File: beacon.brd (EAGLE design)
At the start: 40 x 23.2 mm, 23 parts, among them IC1 MEGA48/88/168-AU, X1 MINI-USB-SCHIELD-32005-301

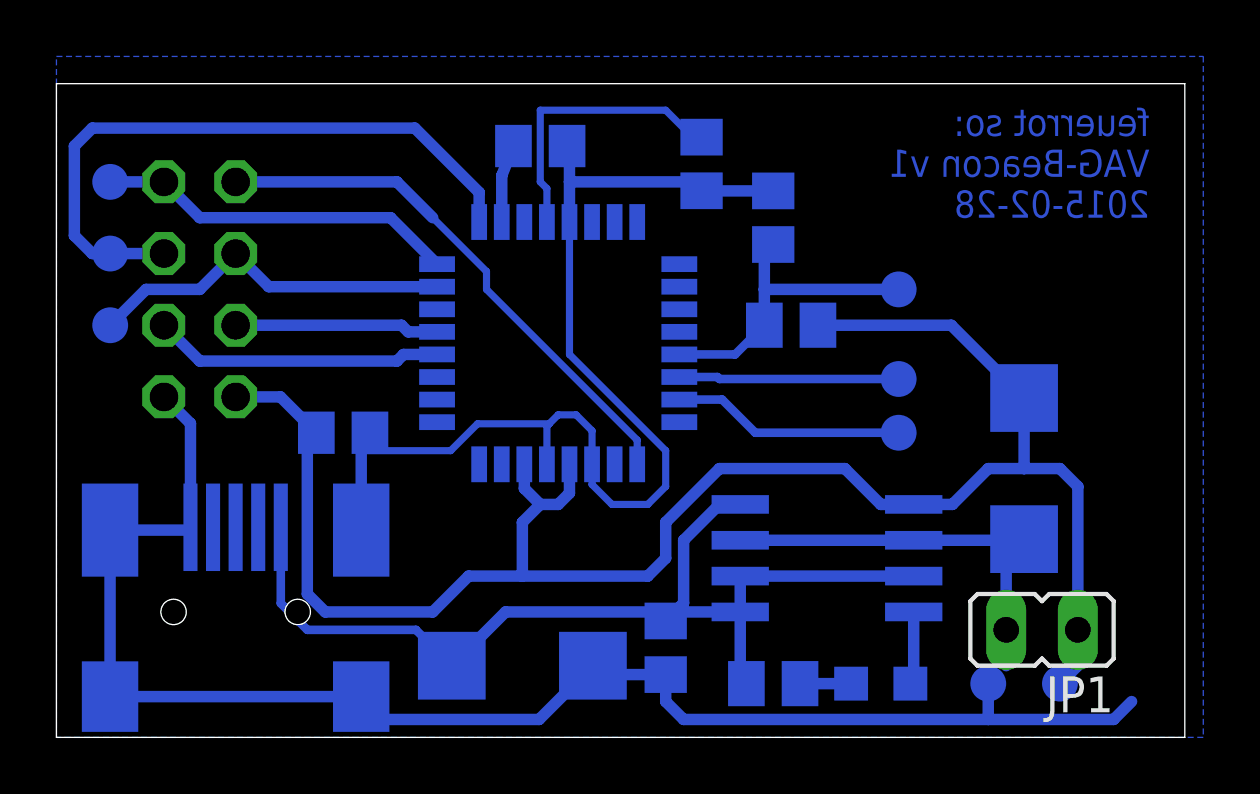
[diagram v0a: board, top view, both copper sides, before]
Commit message: update name+value
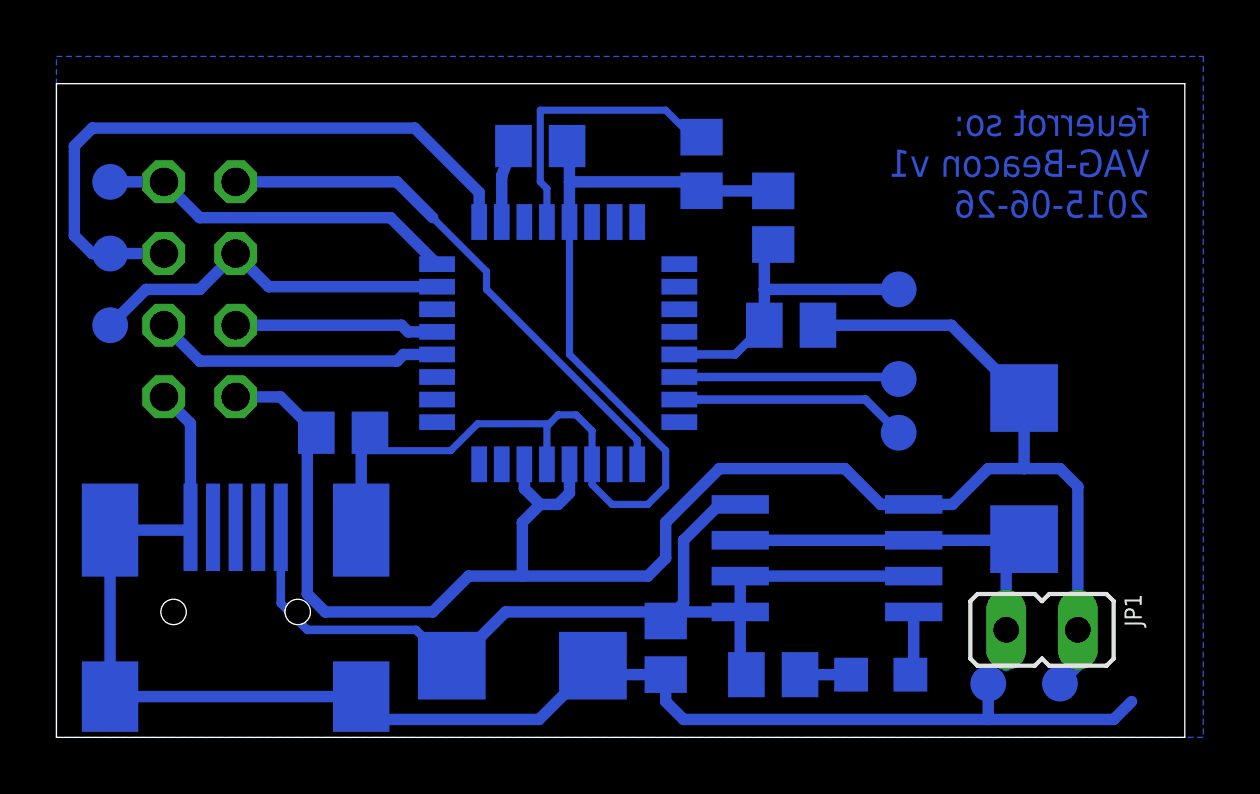
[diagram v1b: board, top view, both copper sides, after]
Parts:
- removed LED1: (no value), led:CHIPLED_0805
- added LED: (no value), led:CHIPLED_0805
- C1, C2: value (none) -> 4.7μF
- C3, C4, C5, C6, C7: value (none) -> 100nF
- IC1: value MEGA48/88/168-AU -> ATMEGA88AU
- R1: value (none) -> 1k
- R6: value (none) -> 10k
- RX, TX: value TPSB1,27 -> (none)
- SV1: value (none) -> nRF24L01+
- USB: value MINI-USB-SCHIELD-32005-301 -> (none)
- moved R1 0.32 mm to (25.4, 2.22)
- renumbered TP1 to RESET, TP2 to MOSI, TP3 to MISO, TP4 to SCK, TP5 to BATT, TP6 to GND, TP7 to RX, TP8 to TX, U$1 to IC2, X1 to USB
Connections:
- net N$1 renamed AVCC
- net N$10 renamed PB1
- net N$11 renamed RESET
- net N$13 renamed PB0
- net N$14 renamed SCK
- net N$15 renamed MISO
- net N$2 renamed RX
- net N$5 renamed TX
- net N$6 renamed INT1
- net N$7 renamed AREF
- net N$9 renamed MOSI
- net N$3: now also LED.A; no longer LED1.A
- net N$4: now also LED.C; no longer LED1.C
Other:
- board text added: "feuerrot so: VAG-Beacon v1 2015-06-26"
- board text removed: "feuerrot so: VAG-Beacon v1 2015-02-28"
